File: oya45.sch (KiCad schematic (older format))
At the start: 94 parts, among them U1 Elite-C

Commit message: Schematics finished final
fixed duplicates
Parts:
- renumbered MX35 to MX46, MX35 to MX47, MX36 to MX48
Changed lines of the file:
@@
 $EndComp
 $Comp
-L MX_Alps_Hybrid:MX-NoLED MX36
+L MX_Alps_Hybrid:MX-NoLED MX48
 U 1 1 61374F37
 P 8050 4850
-F 0 "MX36" H 8083 5073 60  0000 C CNN
+F 0 "MX48" H 8083 5073 60  0000 C CNN
 F 1 "MX-NoLED" H 8083 4999 20  0000 C CNN
 F 2 "" H 7425 4825 60  0001 C CNN
@@
 $EndComp
 $Comp
-L MX_Alps_Hybrid:MX-NoLED MX35
+L MX_Alps_Hybrid:MX-NoLED MX46
 U 1 1 61375469
 P 7550 4850
-F 0 "MX35" H 7583 5073 60  0000 C CNN
+F 0 "MX46" H 7583 5073 60  0000 C CNN
 F 1 "MX-NoLED" H 7583 4999 20  0000 C CNN
 F 2 "" H 6925 4825 60  0001 C CNN
@@
 $EndComp
 $Comp
-L MX_Alps_Hybrid:MX-NoLED MX35
+L MX_Alps_Hybrid:MX-NoLED MX47
 U 1 1 61377FE9
 P 7500 4850
-F 0 "MX35" H 7533 5073 60  0000 C CNN
+F 0 "MX47" H 7533 5073 60  0000 C CNN
 F 1 "MX-NoLED" H 7533 4999 20  0000 C CNN
 F 2 "" H 6875 4825 60  0001 C CNN

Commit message: schematic labeling
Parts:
- D1, D10, D11, D12, D13, D14, D15, D16, D17, D18, D19, D2, D20, D21, D22, D23, D24, D25, D26, D27, D28, D29, D3, D30, D31, D32, D33, D34, D35, D36, D37, D38, D39, D4, D40, D41, D42, D43, D44, D45, D5, D6, D7, D8, D9: footprint (none) -> Keebio-Parts:Diode-Hybrid-Back
- MX1, MX10, MX11, MX12, MX13, MX14, MX15, MX16, MX17, MX18, MX19, MX2, MX20, MX21, MX22, MX23, MX24, MX25, MX26, MX27, MX28, MX29, MX3, MX30, MX31, MX32, MX33, MX34, MX35, MX36, MX37, MX38, MX39, MX4, MX40, MX41, MX42, MX43, MX44, MX45, MX5, MX6, MX7, MX8, MX9: footprint (none) -> MX_Only:MXOnly-1U-Hotswap
- MX46: footprint (none) -> MX_Only:MXOnly-6U-Centered-Hotswap-ReversedStabilizers
- MX47, MX48: footprint (none) -> MX_Only:MXOnly-2U-Hotswap-ReversedStabilizers
- U1: footprint (none) -> Keebio-Parts:Elite-C-castellated-24pin-holes

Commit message: less pads
made a basic pcb instead of complex to make it cheaper
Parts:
- D1, D10, D11, D12, D13, D14, D15, D16, D17, D18, D19, D2, D20, D21, D22, D23, D24, D25, D26, D27, D28, D29, D3, D30, D31, D32, D33, D34, D35, D36, D37, D38, D39, D4, D40, D41, D42, D43, D44, D45, D5, D6, D7, D8, D9: footprint Keebio-Parts:Diode-Hybrid-Back -> Keebio-Parts:Diode
- MX1, MX10, MX11, MX12, MX13, MX14, MX15, MX16, MX17, MX18, MX19, MX2, MX20, MX21, MX22, MX23, MX24, MX25, MX26, MX27, MX28, MX29, MX3, MX30, MX31, MX32, MX33, MX34, MX35, MX36, MX37, MX38, MX39, MX4, MX40, MX41, MX42, MX43, MX44, MX45, MX5, MX6, MX7, MX8, MX9: footprint MX_Only:MXOnly-1U-Hotswap -> MX_Only:MXOnly-1U-NoLED
- MX46: footprint MX_Only:MXOnly-6U-Centered-Hotswap-ReversedStabilizers -> MX_Only:MXOnly-6U-Centered-ReversedStabilizers-NoLED
- MX47, MX48: footprint MX_Only:MXOnly-2U-Hotswap-ReversedStabilizers -> MX_Only:MXOnly-2U-ReversedStabilizers-NoLED
- U1: footprint Keebio-Parts:Elite-C-castellated-24pin-holes -> Keebio-Parts:Elite-C

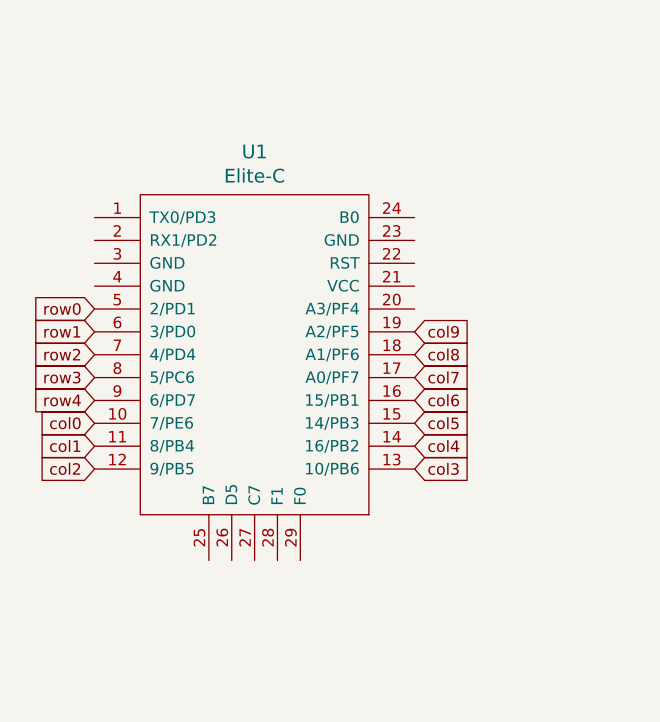
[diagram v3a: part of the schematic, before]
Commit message: added pro micro
pro micro instead of elite c for less pads
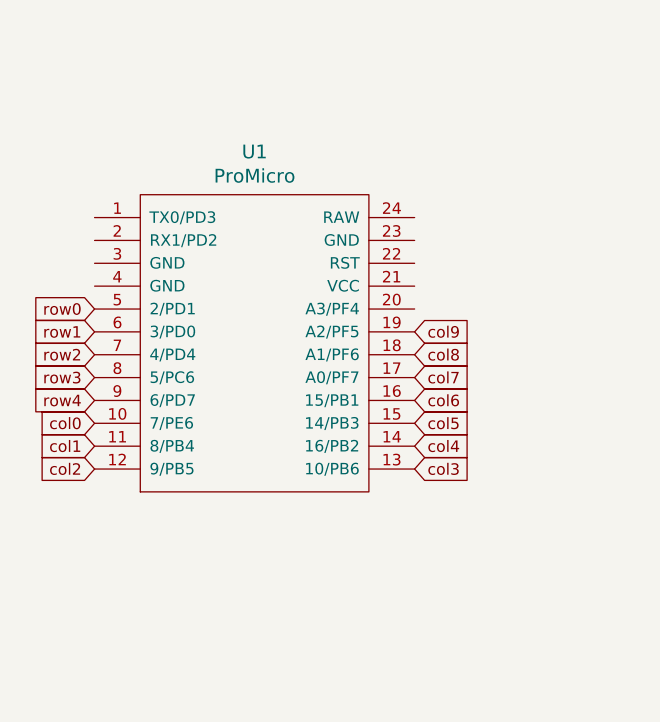
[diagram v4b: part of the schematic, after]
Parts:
- removed U1: Elite-C, Keebio-Parts:Elite-C, symbol keebio:Elite-C
- added U1: ProMicro, Keebio-Parts:ArduinoProMicro, symbol keebio:ProMicro
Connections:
- net col0: now also U1.10 (7/PE6)
- net col1: now also U1.11 (8/PB4)
- net col2: now also U1.12 (9/PB5)
- net col3: now also U1.13 (10/PB6)
- net col4: now also U1.14 (16/PB2)
- net col5: now also U1.15 (14/PB3)
- net col6: now also U1.16 (15/PB1)
- net col7: now also U1.17 (A0/PF7)
- net col8: now also U1.18 (A1/PF6)
- net col9: now also U1.19 (A2/PF5)
- net row0: now also U1.5 (2/PD1)
- net row1: now also U1.6 (3/PD0)
- net row2: now also U1.7 (4/PD4)
- net row3: now also U1.8 (5/PC6)
- net row4: now also U1.9 (6/PD7)
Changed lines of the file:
@@
 $EndDescr
-$Comp
-L keebio:Elite-C U1
-U 1 1 612C7099
-P 3000 3150
-F 0 "U1" H 3000 3987 60  0000 C CNN
-F 1 "Elite-C" H 3000 3881 60  0000 C CNN
-F 2 "Keebio-Parts:Elite-C" V 4050 650 60  0001 C CNN
-F 3 "" V 4050 650 60  0001 C CNN
-	1    3000 3150
-	1    0    0    -1
-$EndComp
 $Comp
 L MX_Alps_Hybrid:MX-NoLED MX5
@@
 	8000 5000 8050 5000
 Connection ~ 8050 5000
+$Comp
+L keebio:ProMicro U1
+U 1 1 612C8517
+P 3000 3150
+F 0 "U1" H 3000 3987 60  0000 C CNN
+F 1 "ProMicro" H 3000 3881 60  0000 C CNN
+F 2 "Keebio-Parts:ArduinoProMicro" V 4050 650 60  0001 C CNN
+F 3 "" V 4050 650 60  0001 C CNN
+	1    3000 3150
+	1    0    0    -1
+$EndComp
 $EndSCHEMATC

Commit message: pro micro first clean routing
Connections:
- net col0: now also U1.13 (10/PB6); no longer U1.10 (7/PE6)
- net col1: now also U1.14 (16/PB2); no longer U1.11 (8/PB4)
- net col2: now also U1.15 (14/PB3); no longer U1.12 (9/PB5)
- net col3: now also U1.16 (15/PB1); no longer U1.13 (10/PB6)
- net col4: now also U1.17 (A0/PF7); no longer U1.14 (16/PB2)
- net col5: now also U1.18 (A1/PF6); no longer U1.15 (14/PB3)
- net col6: now also U1.19 (A2/PF5); no longer U1.16 (15/PB1)
- net col7: now also U1.7 (4/PD4); no longer U1.17 (A0/PF7)
- net col8: now also U1.6 (3/PD0); no longer U1.18 (A1/PF6)
- net col9: now also U1.5 (2/PD1); no longer U1.19 (A2/PF5)
- net row0: now also U1.12 (9/PB5); no longer U1.5 (2/PD1)
- net row1: now also U1.11 (8/PB4); no longer U1.6 (3/PD0)
- net row2: now also U1.10 (7/PE6); no longer U1.7 (4/PD4)
- net row3: now also U1.9 (6/PD7); no longer U1.8 (5/PC6)
- net row4: now also U1.8 (5/PC6); no longer U1.9 (6/PD7)
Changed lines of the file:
@@
 Text GLabel 5250 5200 0    50   Input ~ 0
 row4
+Text GLabel 3700 3400 2    50   Input ~ 0
+col3
+Text GLabel 3700 3300 2    50   Input ~ 0
+col4
+Text GLabel 3700 3200 2    50   Input ~ 0
+col5
+Text GLabel 3700 3100 2    50   Input ~ 0
+col6
+Text GLabel 2300 3200 0    50   Input ~ 0
+col7
+Text GLabel 2300 3100 0    50   Input ~ 0
+col8
 Text GLabel 2300 3000 0    50   Input ~ 0
-row0
-Text GLabel 2300 3100 0    50   Input ~ 0
-row1
-Text GLabel 2300 3200 0    50   Input ~ 0
-row2
-Text GLabel 2300 3300 0    50   Input ~ 0
-row3
-Text GLabel 2300 3400 0    50   Input ~ 0
-row4
-Text GLabel 2300 3500 0    50   Input ~ 0
-col0
-Text GLabel 2300 3600 0    50   Input ~ 0
-col1
-Text GLabel 2300 3700 0    50   Input ~ 0
-col2
-Text GLabel 3700 3700 2    50   Input ~ 0
-col3
-Text GLabel 3700 3600 2    50   Input ~ 0
-col4
-Text GLabel 3700 3500 2    50   Input ~ 0
-col5
-Text GLabel 3700 3400 2    50   Input ~ 0
-col6
-Text GLabel 3700 3300 2    50   Input ~ 0
-col7
-Text GLabel 3700 3200 2    50   Input ~ 0
-col8
-Text GLabel 3700 3100 2    50   Input ~ 0
 col9
 Connection ~ 5750 1800
@@
 	1    0    0    -1
 $EndComp
+Text GLabel 2300 3700 0    50   Input ~ 0
+row0
+Text GLabel 2300 3600 0    50   Input ~ 0
+row1
+Text GLabel 2300 3500 0    50   Input ~ 0
+row2
+Text GLabel 2300 3400 0    50   Input ~ 0
+row3
+Text GLabel 2300 3300 0    50   Input ~ 0
+row4
+Text GLabel 3700 3700 2    50   Input ~ 0
+col0
+Text GLabel 3700 3600 2    50   Input ~ 0
+col1
+Text GLabel 3700 3500 2    50   Input ~ 0
+col2
 $EndSCHEMATC

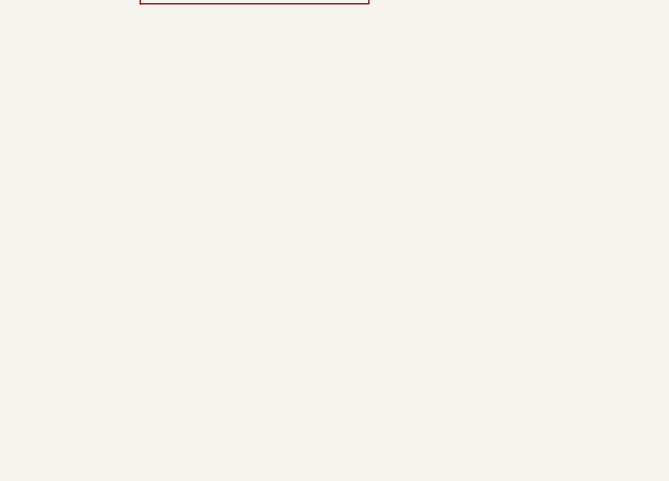
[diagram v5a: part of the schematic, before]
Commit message: added m2 mounting holes
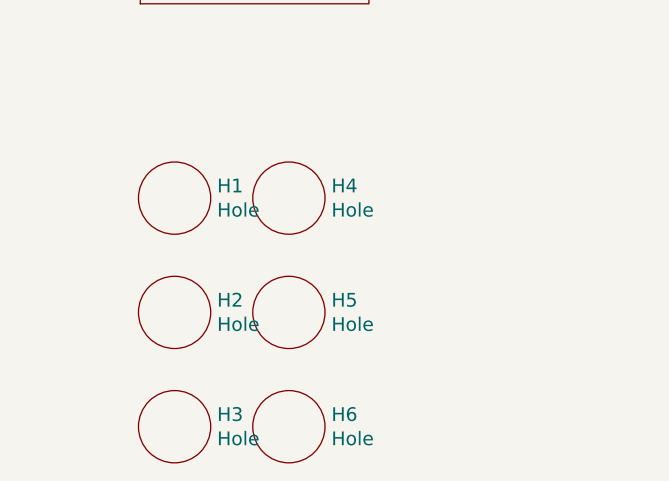
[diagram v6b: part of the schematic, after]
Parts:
- added H1, H2, H3, H4, H5, H6: Hole, kbd:M2_HOLE_v3, symbol keebio:Hole
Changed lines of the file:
@@
 Text GLabel 3700 3500 2    50   Input ~ 0
 col2
+$Comp
+L keebio:Hole H1
+U 1 1 612D2FC8
+P 2650 4650
+F 0 "H1" H 2836 4703 60  0000 L CNN
+F 1 "Hole" H 2836 4597 60  0000 L CNN
+F 2 "kbd:M2_HOLE_v3" H 2650 4650 60  0001 C CNN
+F 3 "" H 2650 4650 60  0001 C CNN
+	1    2650 4650
+	1    0    0    -1
+$EndComp
+$Comp
+L keebio:Hole H4
+U 1 1 612D453E
+P 3150 4650
+F 0 "H4" H 3336 4703 60  0000 L CNN
+F 1 "Hole" H 3336 4597 60  0000 L CNN
+F 2 "kbd:M2_HOLE_v3" H 3150 4650 60  0001 C CNN
+F 3 "" H 3150 4650 60  0001 C CNN
+	1    3150 4650
+	1    0    0    -1
+$EndComp
+$Comp
+L keebio:Hole H2
+U 1 1 612D494A
+P 2650 5150
+F 0 "H2" H 2836 5203 60  0000 L CNN
+F 1 "Hole" H 2836 5097 60  0000 L CNN
+F 2 "kbd:M2_HOLE_v3" H 2650 5150 60  0001 C CNN
+F 3 "" H 2650 5150 60  0001 C CNN
+	1    2650 5150
+	1    0    0    -1
+$EndComp
+$Comp
+L keebio:Hole H5
+U 1 1 612D4EBE
+P 3150 5150
+F 0 "H5" H 3336 5203 60  0000 L CNN
+F 1 "Hole" H 3336 5097 60  0000 L CNN
+F 2 "kbd:M2_HOLE_v3" H 3150 5150 60  0001 C CNN
+F 3 "" H 3150 5150 60  0001 C CNN
+	1    3150 5150
+	1    0    0    -1
+$EndComp
+$Comp
+L keebio:Hole H3
+U 1 1 612D51EF
+P 2650 5650
+F 0 "H3" H 2836 5703 60  0000 L CNN
+F 1 "Hole" H 2836 5597 60  0000 L CNN
+F 2 "kbd:M2_HOLE_v3" H 2650 5650 60  0001 C CNN
+F 3 "" H 2650 5650 60  0001 C CNN
+	1    2650 5650
+	1    0    0    -1
+$EndComp
+$Comp
+L keebio:Hole H6
+U 1 1 612D5571
+P 3150 5650
+F 0 "H6" H 3336 5703 60  0000 L CNN
+F 1 "Hole" H 3336 5597 60  0000 L CNN
+F 2 "kbd:M2_HOLE_v3" H 3150 5650 60  0001 C CNN
+F 3 "" H 3150 5650 60  0001 C CNN
+	1    3150 5650
+	1    0    0    -1
+$EndComp
 $EndSCHEMATC

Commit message: added mounting holes
will have to create plate and bottom plate later. Still deciding how I should mount and what mount points/hole design I should use.
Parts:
- H1, H2, H3, H4, H5, H6: footprint kbd:M2_HOLE_v3 -> kbd:M2_Hole_NPTH_Outside
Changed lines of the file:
@@
 F 0 "H1" H 2836 4703 60  0000 L CNN
 F 1 "Hole" H 2836 4597 60  0000 L CNN
-F 2 "kbd:M2_HOLE_v3" H 2650 4650 60  0001 C CNN
+F 2 "kbd:M2_Hole_NPTH_Outside" H 2650 4650 60  0001 C CNN
 F 3 "" H 2650 4650 60  0001 C CNN
 	1    2650 4650
@@
 F 0 "H4" H 3336 4703 60  0000 L CNN
 F 1 "Hole" H 3336 4597 60  0000 L CNN
-F 2 "kbd:M2_HOLE_v3" H 3150 4650 60  0001 C CNN
+F 2 "kbd:M2_Hole_NPTH_Outside" H 3150 4650 60  0001 C CNN
 F 3 "" H 3150 4650 60  0001 C CNN
 	1    3150 4650
@@
 F 0 "H2" H 2836 5203 60  0000 L CNN
 F 1 "Hole" H 2836 5097 60  0000 L CNN
-F 2 "kbd:M2_HOLE_v3" H 2650 5150 60  0001 C CNN
+F 2 "kbd:M2_Hole_NPTH_Outside" H 2650 5150 60  0001 C CNN
 F 3 "" H 2650 5150 60  0001 C CNN
 	1    2650 5150
@@
 F 0 "H5" H 3336 5203 60  0000 L CNN
 F 1 "Hole" H 3336 5097 60  0000 L CNN
-F 2 "kbd:M2_HOLE_v3" H 3150 5150 60  0001 C CNN
+F 2 "kbd:M2_Hole_NPTH_Outside" H 3150 5150 60  0001 C CNN
 F 3 "" H 3150 5150 60  0001 C CNN
 	1    3150 5150
@@
 F 0 "H3" H 2836 5703 60  0000 L CNN
 F 1 "Hole" H 2836 5597 60  0000 L CNN
-F 2 "kbd:M2_HOLE_v3" H 2650 5650 60  0001 C CNN
+F 2 "kbd:M2_Hole_NPTH_Outside" H 2650 5650 60  0001 C CNN
 F 3 "" H 2650 5650 60  0001 C CNN
 	1    2650 5650
@@
 F 0 "H6" H 3336 5703 60  0000 L CNN
 F 1 "Hole" H 3336 5597 60  0000 L CNN
-F 2 "kbd:M2_HOLE_v3" H 3150 5650 60  0001 C CNN
+F 2 "kbd:M2_Hole_NPTH_Outside" H 3150 5650 60  0001 C CNN
 F 3 "" H 3150 5650 60  0001 C CNN
 	1    3150 5650

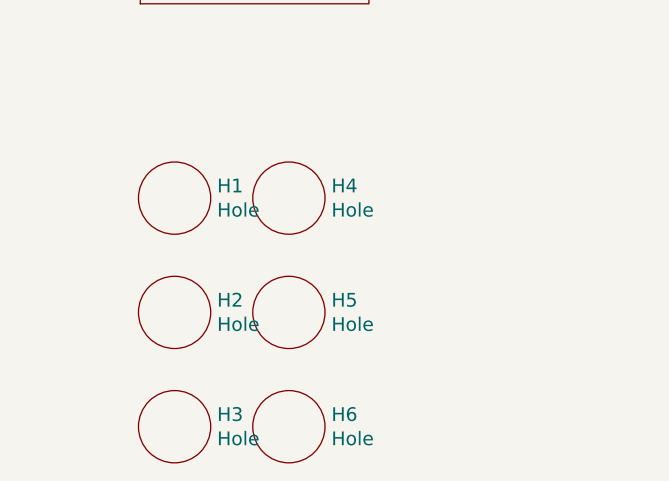
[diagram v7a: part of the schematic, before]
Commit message: diode > smd
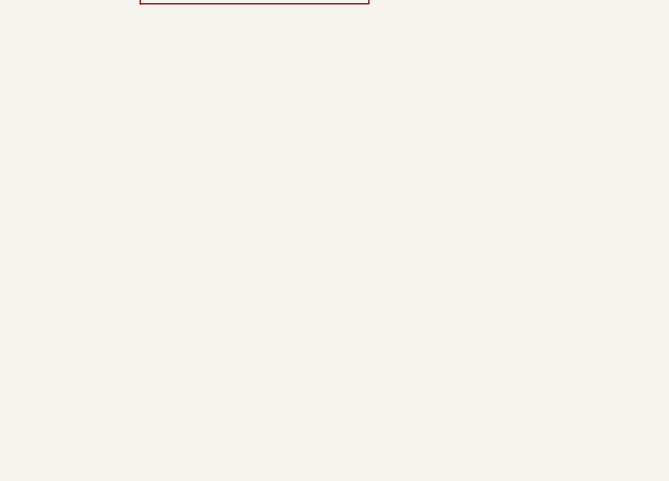
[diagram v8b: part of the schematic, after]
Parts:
- removed H1, H2, H3, H4, H5, H6: Hole, kbd:M2_Hole_NPTH_Outside, symbol keebio:Hole
- D1, D10, D11, D12, D13, D14, D15, D16, D17, D18, D19, D2, D20, D21, D22, D23, D24, D25, D26, D27, D28, D29, D3, D30, D31, D32, D33, D34, D35, D36, D37, D38, D39, D4, D40, D41, D42, D43, D44, D45, D5, D6, D7, D8, D9: footprint Keebio-Parts:Diode -> Keebio-Parts:D_SOD123
